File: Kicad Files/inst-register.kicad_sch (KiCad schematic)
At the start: 20 parts

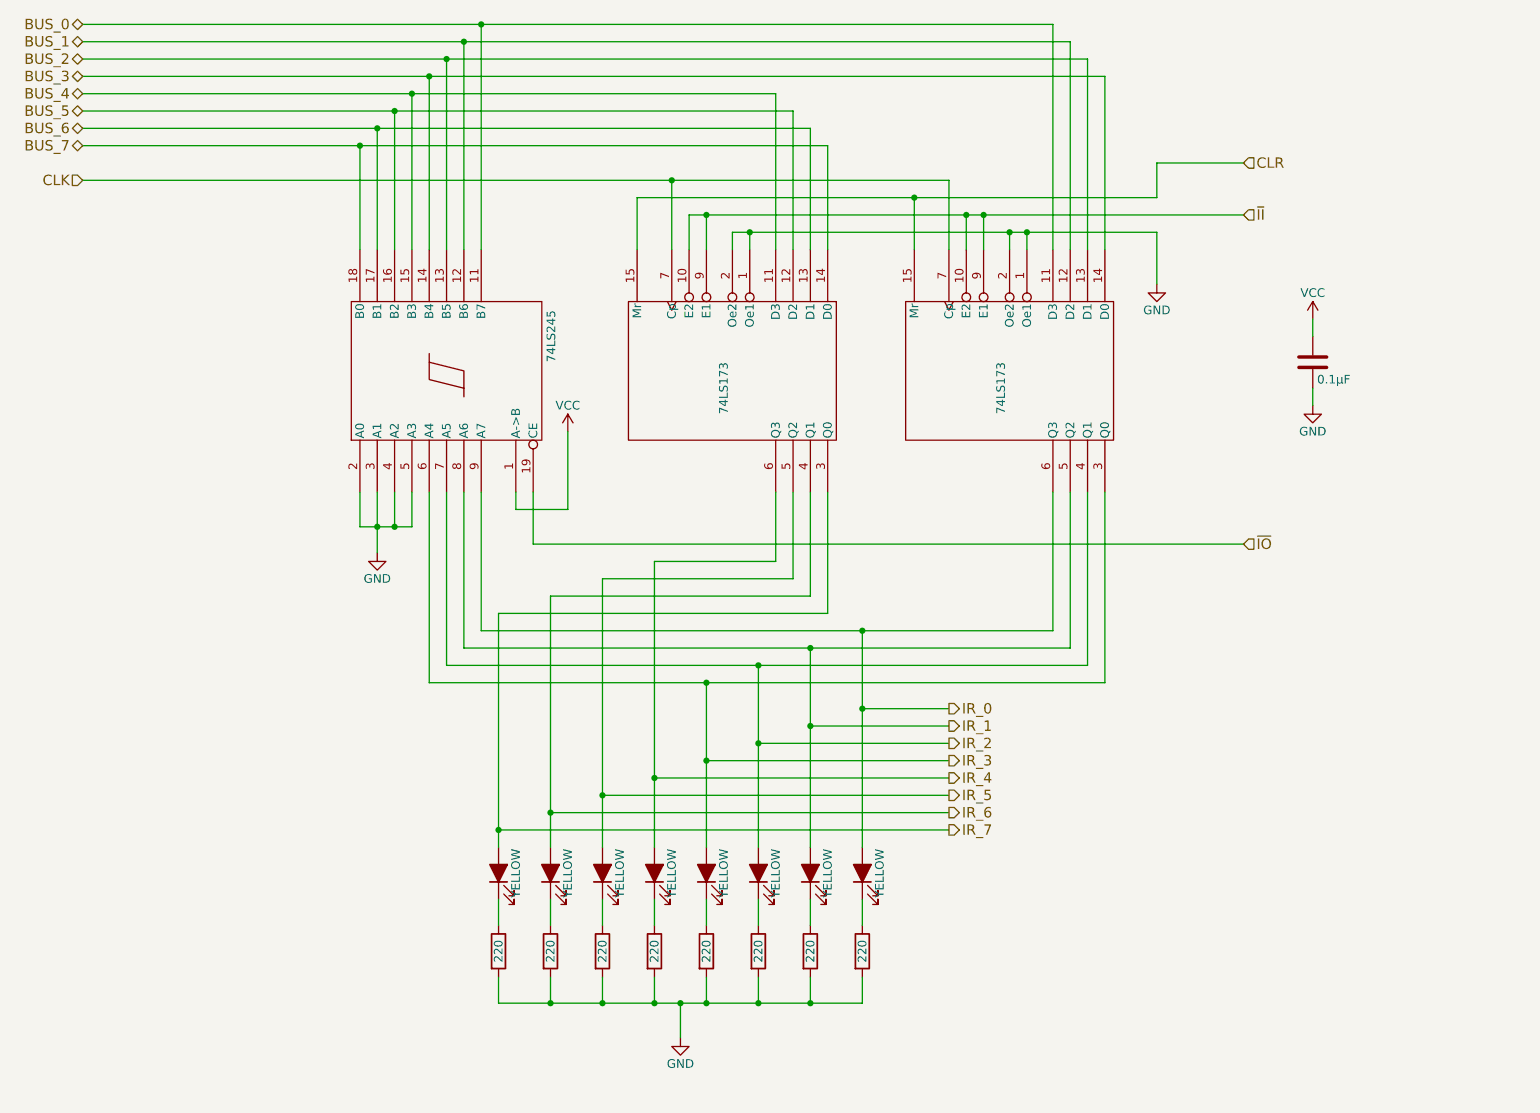
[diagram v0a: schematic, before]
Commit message: started tidy up in control
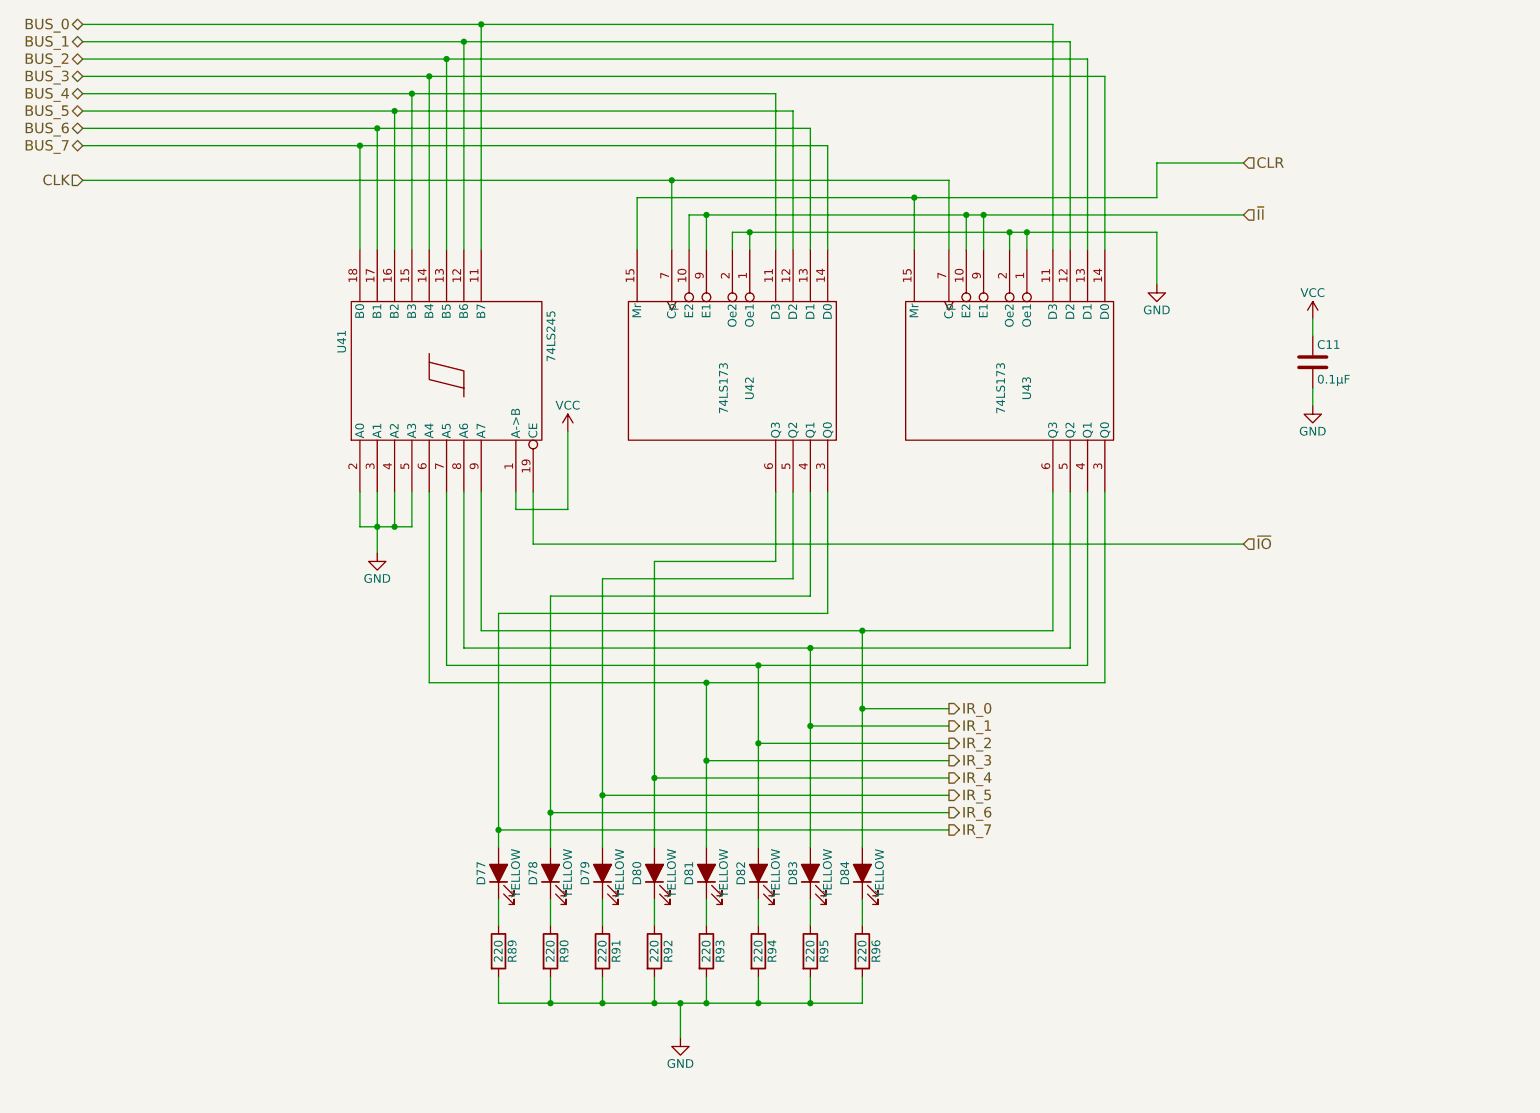
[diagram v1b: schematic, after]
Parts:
- gave numbers to parts that had none: 20
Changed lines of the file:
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@@
   (symbol (lib_id "8bit-computer-rescue:LED_ALT-Device") (at 128.27 138.43 90) (unit 1)
     (in_bom yes) (on_board yes)
-    (property "Reference" "" (id 0) (at 125.73 138.43 0))
+    (property "Reference" "D81" (id 0) (at 125.73 138.43 0))
     (property "Value" "YELLOW" (id 1) (at 130.81 138.43 0))
     (property "Footprint" "LED_THT:LED_D5.0mm" (id 2) (at 128.27 138.43 0)
@@
   (symbol (lib_id "8bit-computer-rescue:LED_ALT-Device") (at 135.89 138.43 90) (unit 1)
     (in_bom yes) (on_board yes)
-    (property "Reference" "" (id 0) (at 133.35 138.43 0))
+    (property "Reference" "D82" (id 0) (at 133.35 138.43 0))
     (property "Value" "YELLOW" (id 1) (at 138.43 138.43 0))
     (property "Footprint" "LED_THT:LED_D5.0mm" (id 2) (at 135.89 138.43 0)
@@
   (symbol (lib_id "Device:R") (at 128.27 149.86 0) (unit 1)
     (in_bom yes) (on_board yes)
-    (property "Reference" "" (id 0) (at 130.302 149.86 90))
+    (property "Reference" "R93" (id 0) (at 130.302 149.86 90))
     (property "Value" "220" (id 1) (at 128.27 149.86 90))
     (property "Footprint" "Resistor_THT:R_Axial_DIN0207_L6.3mm_D2.5mm_P7.62mm_Horizontal" (id 2) (at 126.492 149.86 90)
@@
   (symbol (lib_id "8bit-computer-rescue:74LS173-8bit-computer-rescue") (at 132.08 64.77 270) (unit 1)
     (in_bom yes) (on_board yes)
-    (property "Reference" "" (id 0) (at 134.62 67.31 0))
+    (property "Reference" "U42" (id 0) (at 134.62 67.31 0))
     (property "Value" "74LS173" (id 1) (at 130.81 67.31 0))
     (property "Footprint" "Package_DIP:DIP-16_W7.62mm" (id 2) (at 132.08 64.77 0)
@@
   (symbol (lib_id "8bit-computer-rescue:74LS173-8bit-computer-rescue") (at 172.72 64.77 270) (unit 1)
     (in_bom yes) (on_board yes)
-    (property "Reference" "" (id 0) (at 175.26 67.31 0))
+    (property "Reference" "U43" (id 0) (at 175.26 67.31 0))
     (property "Value" "74LS173" (id 1) (at 171.45 67.31 0))
     (property "Footprint" "Package_DIP:DIP-16_W7.62mm" (id 2) (at 172.72 64.77 0)
@@
   (symbol (lib_id "8bit-computer-rescue:74LS245-8bit-computer-rescue") (at 90.17 64.77 90) (unit 1)
     (in_bom yes) (on_board yes)
-    (property "Reference" "" (id 0) (at 75.565 62.23 0)
+    (property "Reference" "U41" (id 0) (at 75.565 62.23 0)
       (effects (font (size 1.27 1.27)) (justify left bottom))
     )
@@
   (symbol (lib_id "8bit-computer-rescue:LED_ALT-Device") (at 143.51 138.43 90) (unit 1)
     (in_bom yes) (on_board yes)
-    (property "Reference" "" (id 0) (at 140.97 138.43 0))
+    (property "Reference" "D83" (id 0) (at 140.97 138.43 0))
     (property "Value" "YELLOW" (id 1) (at 146.05 138.43 0))
     (property "Footprint" "LED_THT:LED_D5.0mm" (id 2) (at 143.51 138.43 0)
@@
   (symbol (lib_id "8bit-computer-rescue:LED_ALT-Device") (at 151.13 138.43 90) (unit 1)
     (in_bom yes) (on_board yes)
-    (property "Reference" "" (id 0) (at 148.59 138.43 0))
+    (property "Reference" "D84" (id 0) (at 148.59 138.43 0))
     (property "Value" "YELLOW" (id 1) (at 153.67 138.43 0))
     (property "Footprint" "LED_THT:LED_D5.0mm" (id 2) (at 151.13 138.43 0)
@@
   (symbol (lib_id "Device:R") (at 97.79 149.86 0) (unit 1)
     (in_bom yes) (on_board yes)
-    (property "Reference" "" (id 0) (at 99.822 149.86 90))
+    (property "Reference" "R89" (id 0) (at 99.822 149.86 90))
     (property "Value" "220" (id 1) (at 97.79 149.86 90))
     (property "Footprint" "Resistor_THT:R_Axial_DIN0207_L6.3mm_D2.5mm_P7.62mm_Horizontal" (id 2) (at 96.012 149.86 90)
@@
   (symbol (lib_id "Device:R") (at 105.41 149.86 0) (unit 1)
     (in_bom yes) (on_board yes)
-    (property "Reference" "" (id 0) (at 107.442 149.86 90))
+    (property "Reference" "R90" (id 0) (at 107.442 149.86 90))
     (property "Value" "220" (id 1) (at 105.41 149.86 90))
     (property "Footprint" "Resistor_THT:R_Axial_DIN0207_L6.3mm_D2.5mm_P7.62mm_Horizontal" (id 2) (at 103.632 149.86 90)
@@
   (symbol (lib_id "Device:R") (at 113.03 149.86 0) (unit 1)
     (in_bom yes) (on_board yes)
-    (property "Reference" "" (id 0) (at 115.062 149.86 90))
+    (property "Reference" "R91" (id 0) (at 115.062 149.86 90))
     (property "Value" "220" (id 1) (at 113.03 149.86 90))
     (property "Footprint" "Resistor_THT:R_Axial_DIN0207_L6.3mm_D2.5mm_P7.62mm_Horizontal" (id 2) (at 111.252 149.86 90)
@@
   (symbol (lib_id "Device:R") (at 120.65 149.86 0) (unit 1)
     (in_bom yes) (on_board yes)
-    (property "Reference" "" (id 0) (at 122.682 149.86 90))
+    (property "Reference" "R92" (id 0) (at 122.682 149.86 90))
     (property "Value" "220" (id 1) (at 120.65 149.86 90))
     (property "Footprint" "Resistor_THT:R_Axial_DIN0207_L6.3mm_D2.5mm_P7.62mm_Horizontal" (id 2) (at 118.872 149.86 90)
@@
   (symbol (lib_id "Device:R") (at 135.89 149.86 0) (unit 1)
     (in_bom yes) (on_board yes)
-    (property "Reference" "" (id 0) (at 137.922 149.86 90))
+    (property "Reference" "R94" (id 0) (at 137.922 149.86 90))
     (property "Value" "220" (id 1) (at 135.89 149.86 90))
     (property "Footprint" "Resistor_THT:R_Axial_DIN0207_L6.3mm_D2.5mm_P7.62mm_Horizontal" (id 2) (at 134.112 149.86 90)
@@
   (symbol (lib_id "Device:R") (at 143.51 149.86 0) (unit 1)
     (in_bom yes) (on_board yes)
-    (property "Reference" "" (id 0) (at 145.542 149.86 90))
+    (property "Reference" "R95" (id 0) (at 145.542 149.86 90))
     (property "Value" "220" (id 1) (at 143.51 149.86 90))
     (property "Footprint" "Resistor_THT:R_Axial_DIN0207_L6.3mm_D2.5mm_P7.62mm_Horizontal" (id 2) (at 141.732 149.86 90)
@@
   (symbol (lib_id "Device:R") (at 151.13 149.86 0) (unit 1)
     (in_bom yes) (on_board yes)
-    (property "Reference" "" (id 0) (at 153.162 149.86 90))
+    (property "Reference" "R96" (id 0) (at 153.162 149.86 90))
     (property "Value" "220" (id 1) (at 151.13 149.86 90))
     (property "Footprint" "Resistor_THT:R_Axial_DIN0207_L6.3mm_D2.5mm_P7.62mm_Horizontal" (id 2) (at 149.352 149.86 90)
@@
   (symbol (lib_id "Device:C") (at 217.17 63.5 0) (unit 1)
     (in_bom yes) (on_board yes)
-    (property "Reference" "" (id 0) (at 217.805 60.96 0)
+    (property "Reference" "C11" (id 0) (at 217.805 60.96 0)
       (effects (font (size 1.27 1.27)) (justify left))
     )
@@
   (symbol (lib_id "8bit-computer-rescue:LED_ALT-Device") (at 97.79 138.43 90) (unit 1)
     (in_bom yes) (on_board yes)
-    (property "Reference" "" (id 0) (at 95.25 138.43 0))
+    (property "Reference" "D77" (id 0) (at 95.25 138.43 0))
     (property "Value" "YELLOW" (id 1) (at 100.33 138.43 0))
     (property "Footprint" "LED_THT:LED_D5.0mm" (id 2) (at 97.79 138.43 0)
@@
   (symbol (lib_id "8bit-computer-rescue:LED_ALT-Device") (at 105.41 138.43 90) (unit 1)
     (in_bom yes) (on_board yes)
-    (property "Reference" "" (id 0) (at 102.87 138.43 0))
+    (property "Reference" "D78" (id 0) (at 102.87 138.43 0))
     (property "Value" "YELLOW" (id 1) (at 107.95 138.43 0))
     (property "Footprint" "LED_THT:LED_D5.0mm" (id 2) (at 105.41 138.43 0)
@@
   (symbol (lib_id "8bit-computer-rescue:LED_ALT-Device") (at 113.03 138.43 90) (unit 1)
     (in_bom yes) (on_board yes)
-    (property "Reference" "" (id 0) (at 110.49 138.43 0))
+    (property "Reference" "D79" (id 0) (at 110.49 138.43 0))
     (property "Value" "YELLOW" (id 1) (at 115.57 138.43 0))
     (property "Footprint" "LED_THT:LED_D5.0mm" (id 2) (at 113.03 138.43 0)
@@
   (symbol (lib_id "8bit-computer-rescue:LED_ALT-Device") (at 120.65 138.43 90) (unit 1)
     (in_bom yes) (on_board yes)
-    (property "Reference" "" (id 0) (at 118.11 138.43 0))
+    (property "Reference" "D80" (id 0) (at 118.11 138.43 0))
     (property "Value" "YELLOW" (id 1) (at 123.19 138.43 0))
     (property "Footprint" "LED_THT:LED_D5.0mm" (id 2) (at 120.65 138.43 0)

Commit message: work on cl
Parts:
- C21: renamed from C11; value 0.1µF -> C
- R100: renamed from R96; value 220 -> R
- R93: renamed from R89; value 220 -> R
- R94: renamed from R90; value 220 -> R
- R95: renamed from R91; value 220 -> R
- R96: renamed from R92; value 220 -> R
- R97: renamed from R93; value 220 -> R
- R98: renamed from R94; value 220 -> R
- R99: renamed from R95; value 220 -> R
- renumbered D77 to D58, D78 to D59, D79 to D60, D80 to D61, D81 to D62, D82 to D63, D83 to D64, D84 to D65, U41 to U42, U42 to U43, U43 to U44

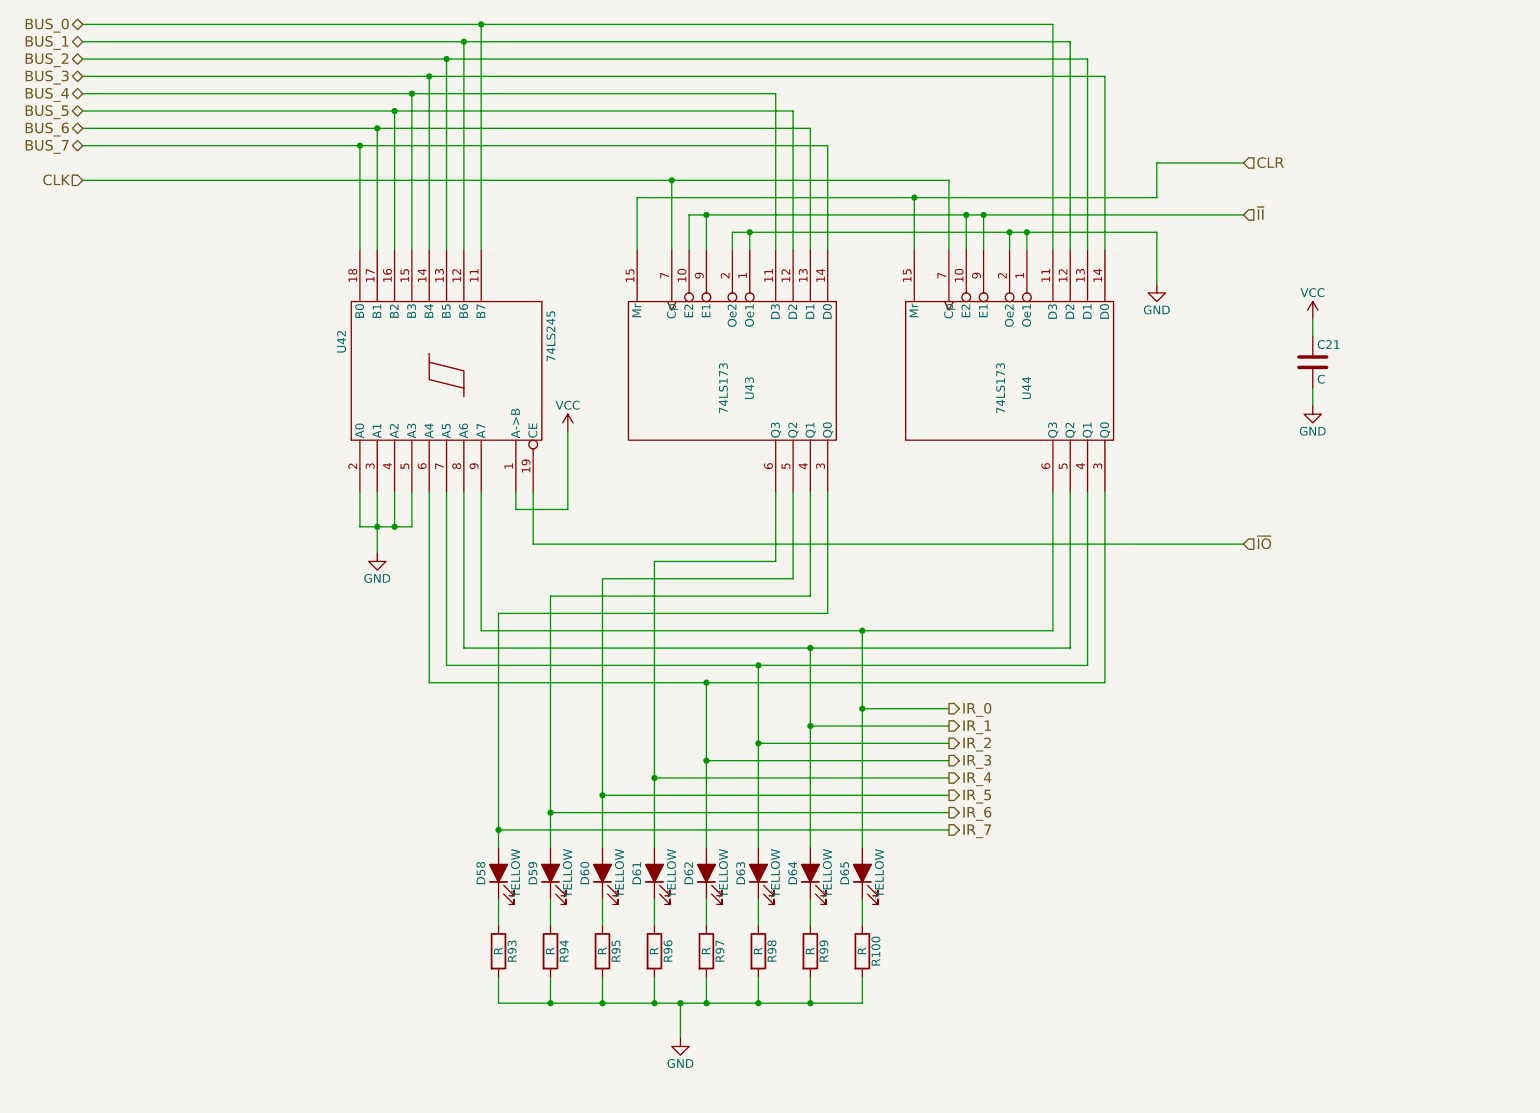
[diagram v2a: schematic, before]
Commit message: fixed ecc problems
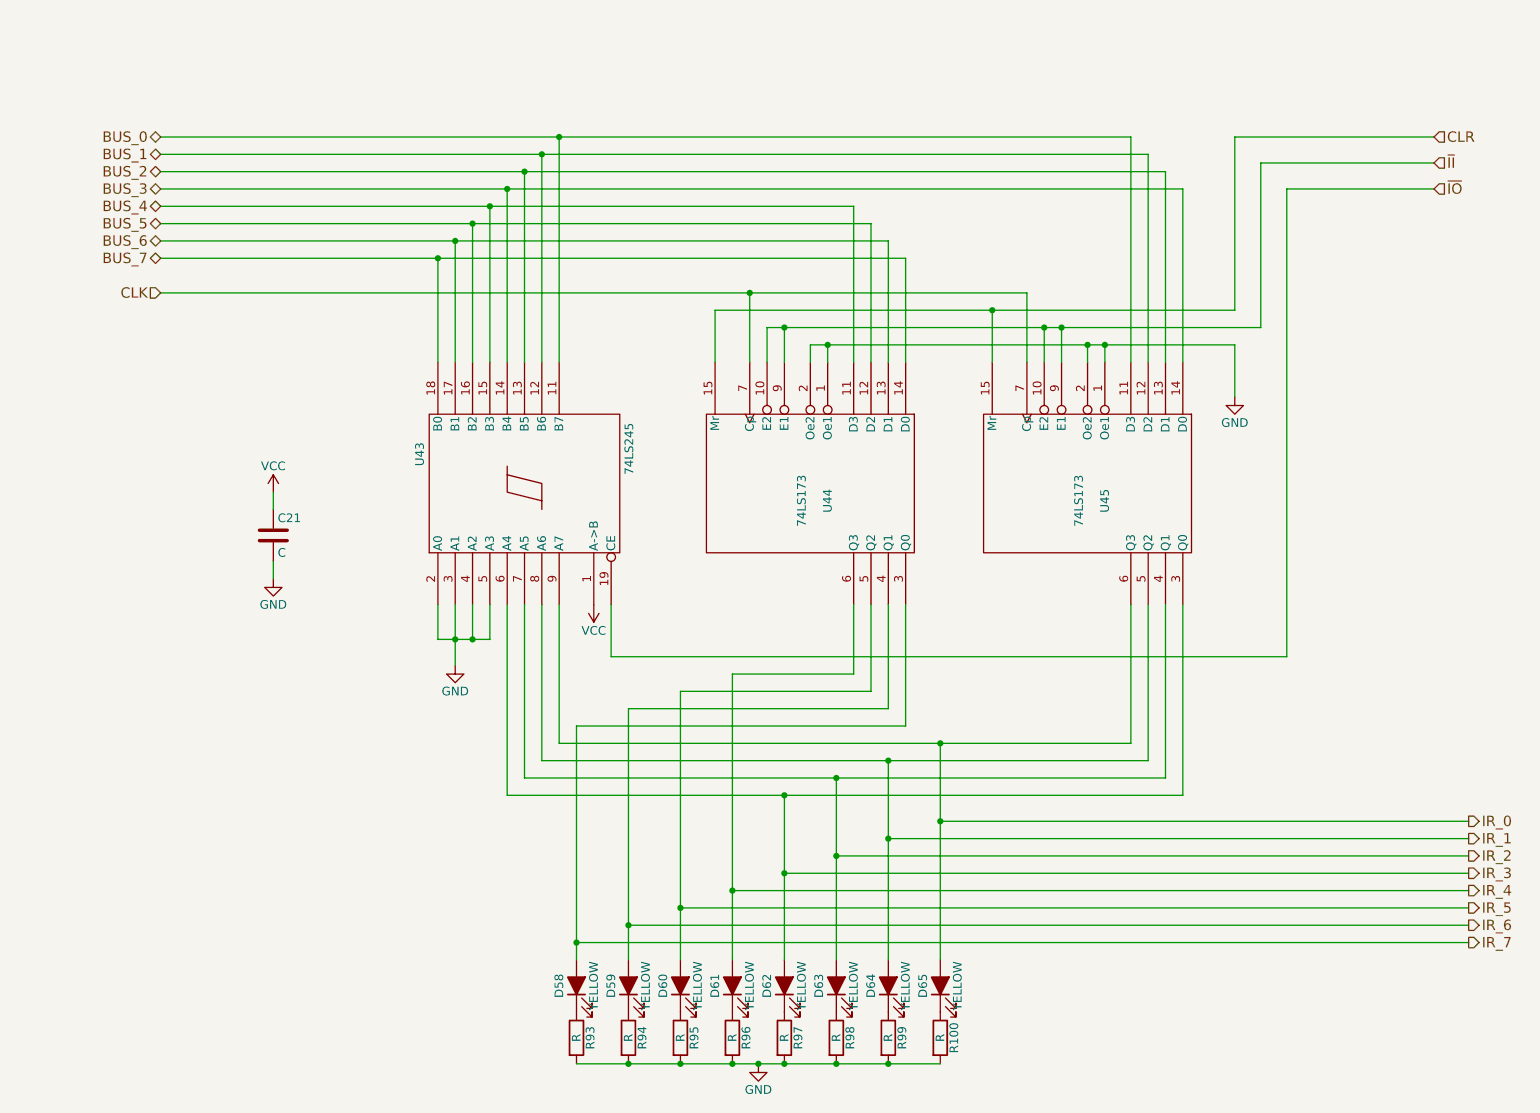
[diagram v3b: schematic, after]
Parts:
- renumbered U42 to U43, U43 to U44, U44 to U45
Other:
- moved on the sheet: C21, D58, D59, D60, D61, D62, D63, D64, D65, R100, R93, R94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
